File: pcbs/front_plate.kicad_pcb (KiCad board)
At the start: 2 copper layers, 73 x 111 mm, 1 part

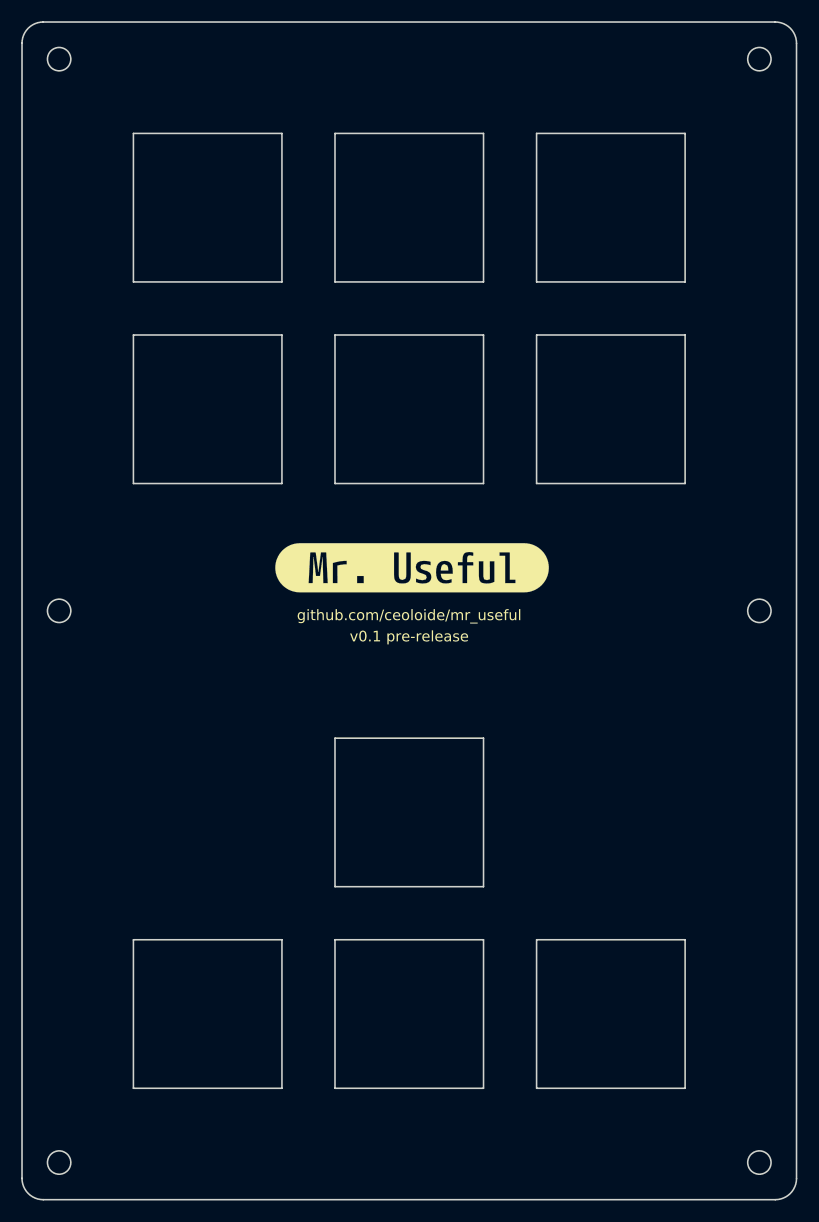
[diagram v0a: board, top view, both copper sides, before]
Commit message: Update MX switch footprint
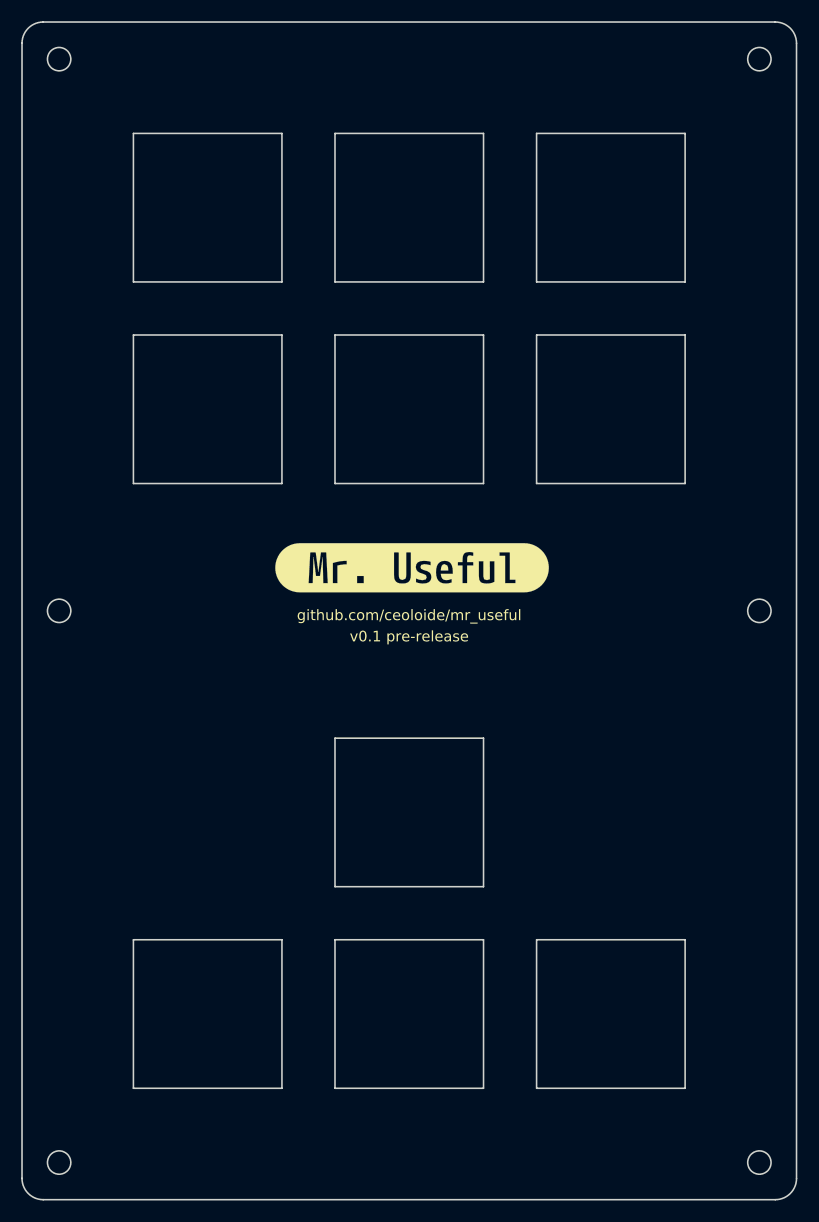
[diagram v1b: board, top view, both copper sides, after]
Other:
- net class Default removed
